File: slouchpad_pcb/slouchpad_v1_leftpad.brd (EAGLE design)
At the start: 17.8 x 33 mm, 47 parts, among them U2 MIC5219, U3 ATMEGA32U4, Y1 16MHz

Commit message: Retooled the project to be a modular joypad
Rather than being a shield for the SparkFun Pro Micro Arduino, the slouchpad will simply be a modular joypad for use with any microcontroller.

Modified the license to reflect the removal of the SparkFun Pro Micro

Removed backup design files

Created button layout for left thumb pad

Modified all board positions to units of mm where possible.

Signed-off-by: Eric Jones <eric.r.k.jones@gmail.com>
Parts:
- removed C1, C3: 0.1uF, SparkFun:0603-CAP
- removed C10, C5, C6: 1uF, SparkFun:0603-CAP
- removed C13, C19: 10uF, SparkFun:EIA3216
- removed C2, C4: 22pF, SparkFun:0603-CAP
- removed D1: Yellow, SparkFun:LED-0603
- removed D2: (no value), SparkFun:SOD-323
- removed D3: Green, SparkFun:LED-0603
- removed F1: 500mA, SparkFun:PTC-1206
- removed FRAME1: FRAME-LETTER, SparkFun-Aesthetics:CREATIVE_COMMONS
- removed JP3: (no value), pinhead:1X03
- removed JP4: (no value), pinhead:1X13
- removed JP6, JP7: (no value), SparkFun:1X12
- removed LED1: Red, SparkFun:LED-0603
- removed R10: 10K, resistor:M1206
- removed R11: 1K, SparkFun:0603-RES
- removed R5, R7: 22, SparkFun:0603-RES
- removed R6: 330, SparkFun:0603-RES
- removed R8: 33K, resistor:M1206
- removed R9: 47K, resistor:M1206
- removed SJ1: Closed for 5V Board, SparkFun:SJ_2S
- removed U$1: LOGO-SFESK, SparkFun:SFE-LOGO-FLAME
- removed U$11: LOGO-SFENEW, SparkFun:SFE-NEW-WEBLOGO
- removed U$3: OSHW-LOGOS, SparkFun:OSHW-LOGO-S
- removed U2: MIC5219, SparkFun:SOT23-5
- removed U3: ATMEGA32U4, Testing:QFN-44-NOPAD_1:1-OUTFAKES
- removed X1: (no value), Testing:USB-AB-MICRO-SMD-V03-IN&OUT
- removed Y1: 16MHz, SparkFun:CRYSTAL-SMD-5X3
- JP1: value FIDUCIALUFIDUCIAL -> (none); device SparkFun:MICRO-FIDUCIAL -> pinhead:1X13
- JP2: value FIDUCIALUFIDUCIAL -> (none); device SparkFun:MICRO-FIDUCIAL -> pinhead:1X03
- R1: value 10K -> (none); device resistor:M1206 -> resistor:0204/5
- R2: value 10K -> (none); device SparkFun:0603-RES -> resistor:0204/5
- R3: value 22K -> (none); device resistor:M1206 -> resistor:0204/5
- R4: value 330 -> (none); device SparkFun:0603-RES -> resistor:0204/5
- moved MENU 218.8 mm to (8.00, 60.0), turned to 225 degrees
- moved R3 204.1 mm to (6.00, 22.0)
- moved SELECT 203.2 mm to (33.0, 60.0), turned to 135 degrees
- moved R1 200.5 mm to (6.00, 26.0)
- moved RIGHT 137.0 mm to (27.0, 13.5), turned to 315 degrees
- moved LEFT 112.1 mm to (14.0, 13.5), turned to 315 degrees
- moved JOY1 90.1 mm to (20.5, 48.0)
- moved DOWN 89.5 mm to (20.5, 7.00), turned to 45 degrees
- moved UP 82.3 mm to (20.5, 20.0), turned to 45 degrees
- moved JP1 43.9 mm to (38.2, 36.5), turned to 270 degrees
- moved JP2 39.3 mm to (20.5, 65.0)
- moved R4 35.8 mm to (30.0, 27.0), turned to 180 degrees
- moved R2 25.2 mm to (30.0, 24.0), turned to 180 degrees
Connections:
- removed net A0: DOWN.3, DOWN.4, JP6.8, LEFT.3, LEFT.4, R10.1, RIGHT.3, RIGHT.4, U3.36, UP.3, UP.4
- removed net A1: JOY1.X, JP6.7, U3.37
- removed net A2: JOY1.Y, JP6.6, U3.38
- removed net A3: JP6.5, U3.39
- removed net A4: U3.40
- removed net A5: U3.41
- removed net AREF: C1.2, U3.42
- removed net D+: R5.1, U3.4
- removed net D-: R7.1, U3.3
- removed net D10: JP6.12, U3.30
- removed net D11: U3.12
- removed net D12: U3.26
- removed net D13: U3.32
- removed net D14: R4.1, U3.8
- removed net D2: JP7.8, U3.19
- removed net D3: JP7.7, U3.18
- removed net D4: JP7.6, U3.25
- removed net D5: JP7.5, U3.31
- removed net D6: JP7.4, U3.27
- removed net D7: JP7.3, U3.1
- removed net D8: JP7.2, U3.28
- removed net D9: JP7.1, U3.29
- removed net MISO: JP6.10, U3.11
- removed net MOSI: JP6.11, U3.10
- removed net N$1: C4.1, U3.16, Y1.1
- removed net N$10: DOWN.1, DOWN.2, R3.1
- removed net N$11: LEFT.1, LEFT.2, R8.1
- removed net N$12: R9.1, RIGHT.1, RIGHT.2
- removed net N$14: SELECT.3, SELECT.4
- removed net N$15: MENU.3, MENU.4
- removed net N$38: LED1.A, R11.1
- removed net N$4: C5.2, U3.6
- removed net N$5: D1.C, R4.2
- removed net N$6: R7.2, X1.D-1
- removed net N$7: D3.C, R6.2
- removed net N$8: R5.2, X1.D+1
- removed net N$9: R1.1, UP.1, UP.2
- removed net RAW: C19.A, D2.1, JP6.1, U2.1, U2.3
- removed net RESET: JP6.3, R2.1, U3.13
- removed net RXI: JP7.11, U3.20
- removed net SCK: JP6.9, U3.9
- removed net TXLED: R6.1, U3.22
- removed net TXO: JP7.12, U3.21
- removed net UVCC: C6.2, F1.1, U3.2, U3.7, X1.VBUS1
- new net A: JP1.7
- new net B: JP1.8
- new net C: JP1.9
- new net DOWN: DOWN.1, DOWN.2, R2.2
- new net JOYX: JOY1.X, JP1.12
- new net JOYY: JOY1.Y, JP1.10
- new net LEFT: LEFT.1, LEFT.2, R3.2
- new net MENU: MENU.1, MENU.2
- new net RIGHT: R4.2, RIGHT.1, RIGHT.2
- new net SELECT: SELECT.1, SELECT.2
- new net START: JP1.1
- new net UP: R1.2, UP.1, UP.2
- new net X: JP1.6
- new net Y: JP1.5
- new net Z: JP1.4
- net GND: now also DOWN.3, DOWN.4, JP1.13, JP2.2, LEFT.3, LEFT.4, MENU.3, MENU.4, RIGHT.3, RIGHT.4, SELECT.3, SELECT.4, UP.3, UP.4; no longer C1.1, C10.2, C13.C, C19.C, C2.2, C3.1, C4.2, C5.1, C6.1, JP6.2, JP7.10, JP7.9, LED1.C, MENU.1, MENU.2, R1.2, R3.2, R8.2, R9.2, SELECT.1, SELECT.2, U2.2, U3.15, U3.23, U3.33, U3.35, U3.43, U3.5, X1.GND1
- net N$2: now also JP1.2, JP2.1; no longer C2.1, U3.17, Y1.3
- net N$3: now also JP1.3, JP2.3; no longer D2.2, F1.2, SJ1.1
- net VCC: now also JP1.11; no longer C10.1, C13.A, C3.2, D1.A, D3.A, JP6.4, R10.2, R11.2, R2.2, SJ1.2, U2.5, U3.14, U3.24, U3.34, U3.44
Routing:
- net VCC: track 83.7 -> 0.00 mm, vias 4 -> 0
- net RESET: track 44.6 -> 0.00 mm, vias 1 -> 0
- net UVCC: track 33.6 -> 0.00 mm, vias 4 -> 0
- net D7: track 32.8 -> 0.00 mm, vias 2 -> 0
- net TXO: track 28.8 -> 0.00 mm, vias 1 -> 0
- net D-: track 28.7 -> 0.00 mm, vias 2 -> 0
- net D2: track 27.8 -> 0.00 mm, vias 1 -> 0
- net D5: track 27.6 -> 0.00 mm, vias 1 -> 0
- net RXI: track 27.1 -> 0.00 mm, vias 1 -> 0
- net D9: track 26.9 -> 0.00 mm, vias 1 -> 0
- net D8: track 26.6 -> 0.00 mm, vias 1 -> 0
- net RAW: track 25.8 -> 0.00 mm, vias 1 -> 0
- net D+: track 24.6 -> 0.00 mm, vias 2 -> 0
- net D6: track 23.2 -> 0.00 mm, vias 1 -> 0
- net D4: track 22.3 -> 0.00 mm, vias 1 -> 0
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- removed copper zone on layer 16, net GND
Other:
- board size 17.8 x 33 mm -> 41 x 69 mm
- board text removed: "10"
- board text removed: "14"
- board text removed: "15"
- board text removed: "16"
- board text removed: "2"
- board text removed: "3"
- board text removed: "3.3V"
- board text removed: "3.3V Reg / 8MHz"
- board text removed: "4"
- board text removed: "5"
- board text removed: "5V"
- board text removed: "5V Reg / 16MHz"
- board text removed: "6"
- board text removed: "7"
- board text removed: "8"
- board text removed: "9"
- board text removed: "A0"
- board text removed: "A1"
- board text removed: "A2"
- board text removed: "A3"
- board text removed: "GND"
- board text removed: "J1"
- board text removed: "Mark back accordingly"
- board text removed: "Micro"
- board text removed: "N. Seidle, revised by P. Lewis"
- board text removed: "Pro"
- board text removed: "RAW"
- board text removed: "RST"
- board text removed: "RXI"
- board text removed: "TXO"
- board text removed: "VCC"
- board text removed: "Valid combinations:"
- board text removed: "v13"

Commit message: Finished board layouts
Cleaned up schematics
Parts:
- added R5: 10K, resistor:0204/5
- JP1: device pinhead:1X13 -> pinhead:1X09
- R1: value (none) -> 10K
- R2: value (none) -> 22K
- R3: value (none) -> 33K
- R4: value (none) -> 47K
- moved R3 24.6 mm to (30.1, 26.6), turned to 225 degrees
- moved R1 21.6 mm to (27.3, 29.5), turned to 225 degrees
- moved JP1 6.35 mm to (38.2, 42.9)
- moved R2 4.25 mm to (28.7, 28.1), turned to 225 degrees
- moved R4 2.36 mm to (31.6, 25.2), turned to 225 degrees
- turned DOWN to 135 degrees
- turned JOY1 to 180 degrees
- turned LEFT to 45 degrees
- turned RIGHT to 45 degrees
- turned UP to 135 degrees
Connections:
- removed net A: JP1.7
- removed net B: JP1.8
- removed net C: JP1.9
- removed net DOWN: DOWN.1, DOWN.2, R2.2
- removed net LEFT: LEFT.1, LEFT.2, R3.2
- removed net RIGHT: R4.2, RIGHT.1, RIGHT.2
- removed net START: JP1.1
- removed net UP: R1.2, UP.1, UP.2
- removed net X: JP1.6
- removed net Y: JP1.5
- removed net Z: JP1.4
- new net DPAD: JP1.8, R1.1, R2.1, R3.1, R4.1, R5.2
- new net N$1: JP1.2, JP2.3
- new net N$4: R3.2, RIGHT.1, RIGHT.2
- new net N$5: DOWN.1, DOWN.2, R4.2
- new net N$6: R2.2, UP.1, UP.2
- net GND: now also JP1.9; no longer JP1.13
- net JOYX: now also JP1.7; no longer JP1.12
- net JOYY: now also JP1.5; no longer JP1.10
- net MENU: now also JP1.4
- net N$2: now also JP1.3; no longer JP1.2
- net N$3: now also LEFT.1, LEFT.2, R1.2; no longer JP1.3, JP2.3
- net SELECT: now also JP1.1
- net VCC: now also JP1.6, R5.1; no longer JP1.11
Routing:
- net VCC: track 0.00 -> 37.8 mm
- net MENU: track 0.00 -> 33.0 mm
- net JOYY: track 0.00 -> 29.9 mm
- net N$5: track 0.00 -> 25.2 mm
- net JOYX: track 0.00 -> 24.7 mm
- net DPAD: track 0.00 -> 22.0 mm
- net N$1: track 0.00 -> 22.0 mm
- net N$3: track 0.00 -> 14.2 mm
- net N$6: track 0.00 -> 12.9 mm
- net N$4: track 0.00 -> 6.85 mm
- net SELECT: track 0.00 -> 4.91 mm

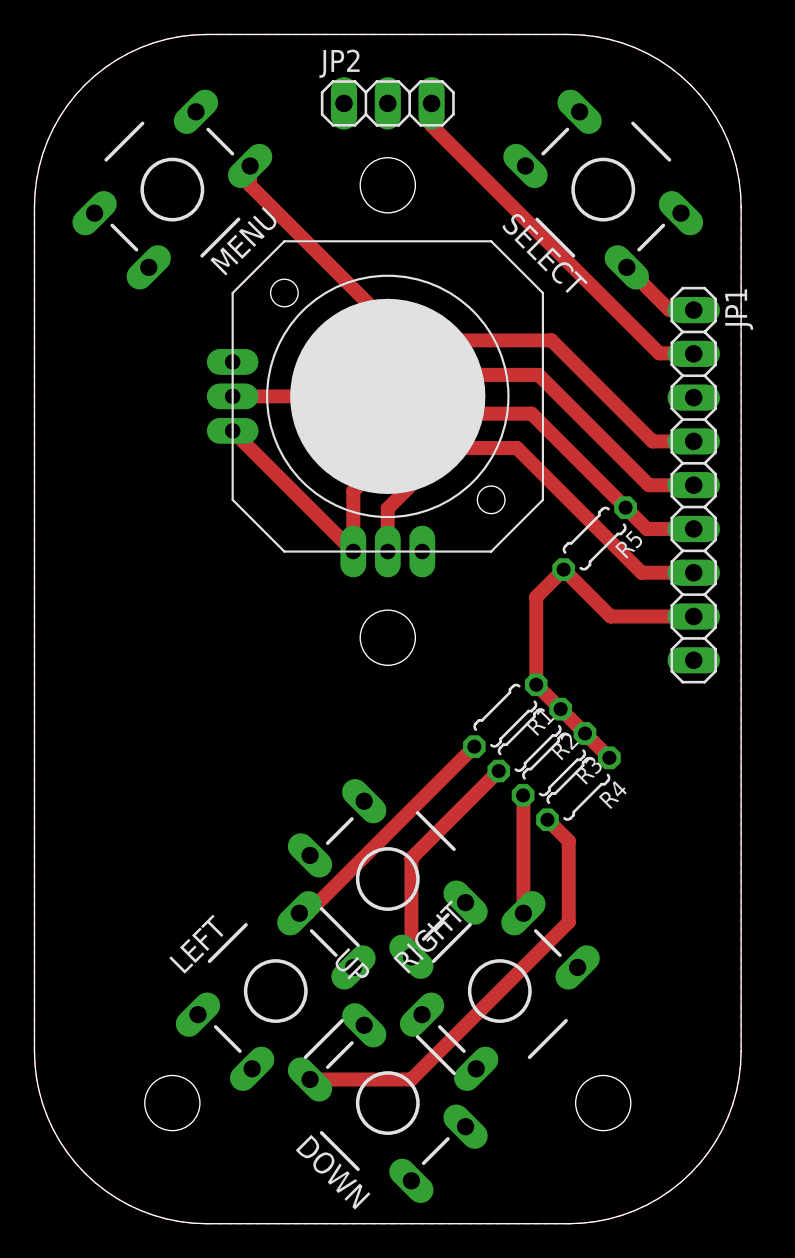
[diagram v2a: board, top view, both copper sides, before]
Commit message: Finished silkscreen of boards
Moved traces to bottom layer to represent design intention
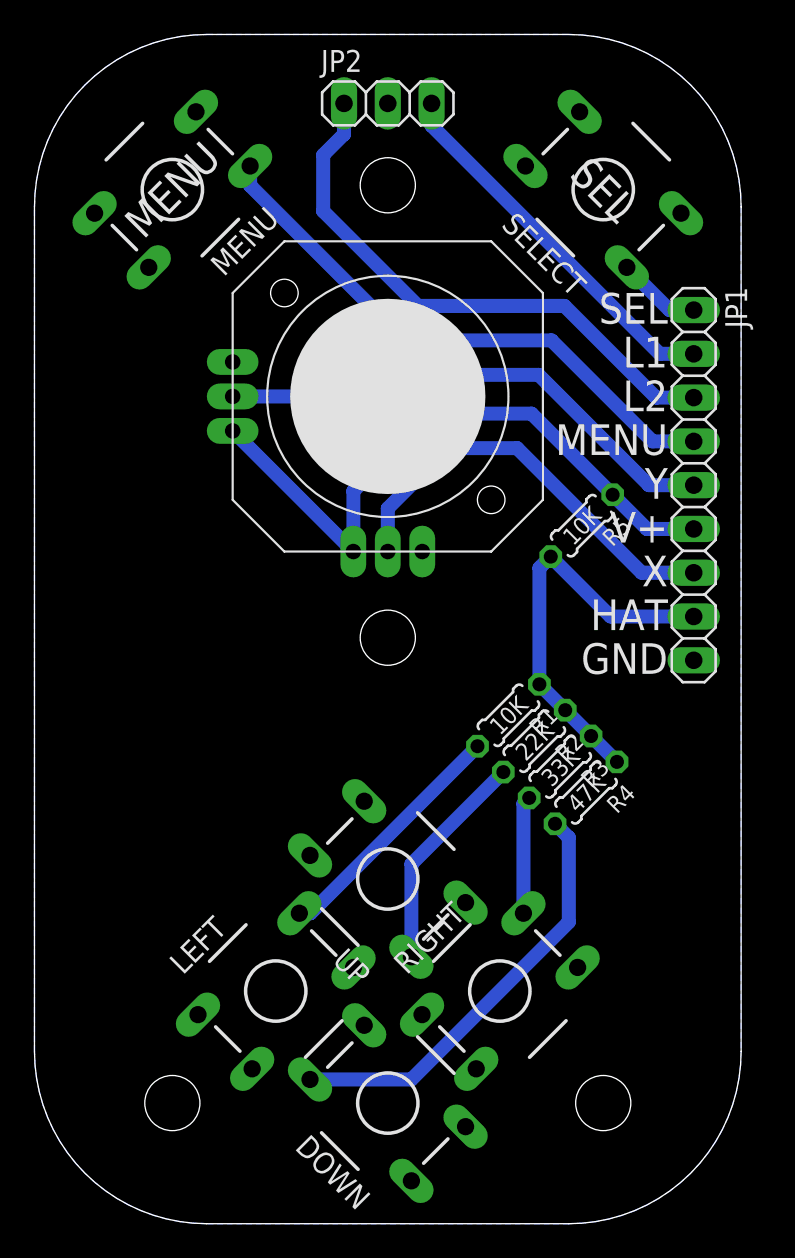
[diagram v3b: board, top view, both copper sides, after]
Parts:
- moved R5 1.06 mm to (31.8, 40.5)
- moved R4 0.50 mm to (32.0, 25.0)
- moved R3 0.38 mm to (30.5, 26.5)
- moved R2 0.27 mm to (29.0, 28.0)
- moved R1 0.18 mm to (27.5, 29.5)
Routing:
- net N$2: track 0.00 -> 32.7 mm
- net DPAD: track 22.0 -> 23.8 mm
- added copper zone on layer 16, net GND
- removed copper zone on layer 1, net GND
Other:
- board text added: "10K"
- board text added: "22K"
- board text added: "33K"
- board text added: "47K"
- board text added: "GND"
- board text added: "HAT"
- board text added: "L1"
- board text added: "L2"
- board text added: "MENU"
- board text added: "SEL"
- board text added: "V+"
- board text added: "X"
- board text added: "Y"
